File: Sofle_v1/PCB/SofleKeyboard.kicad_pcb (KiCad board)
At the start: 2 copper layers, 137.2 x 109.2 mm, 87 parts, among them J1 LED, J2 4PIN, J3 OLED, P1 i2c_pin, P2 i2c_pin, SW1 SW_PUSH, SW10 SW_PUSH, SW11 SW_PUSH, SW12 SW_PUSH, SW13 SW_PUSH, SW14 SW_PUSH, SW15 SW_PUSH, SW16 SW_PUSH, SW17 SW_PUSH, SW18 SW_PUSH, SW19 SW_PUSH, SW2 SW_PUSH, SW20 SW_PUSH, SW21 SW_PUSH, SW22 SW_PUSH, SW23 SW_PUSH, SW24 SW_PUSH, SW25 Rotary_Encoder_Switch, SW26 SW_PUSH, SW27 SW_PUSH, SW28 SW_PUSH, SW29 SW_PUSH, SW3 SW_PUSH, SW30 SW_PUSH, SW4 SW_PUSH, SW5 SW_PUSH, SW6 SW_PUSH, SW7 SW_PUSH, SW8 SW_PUSH, SW9 SW_PUSH, U1 ProMicro

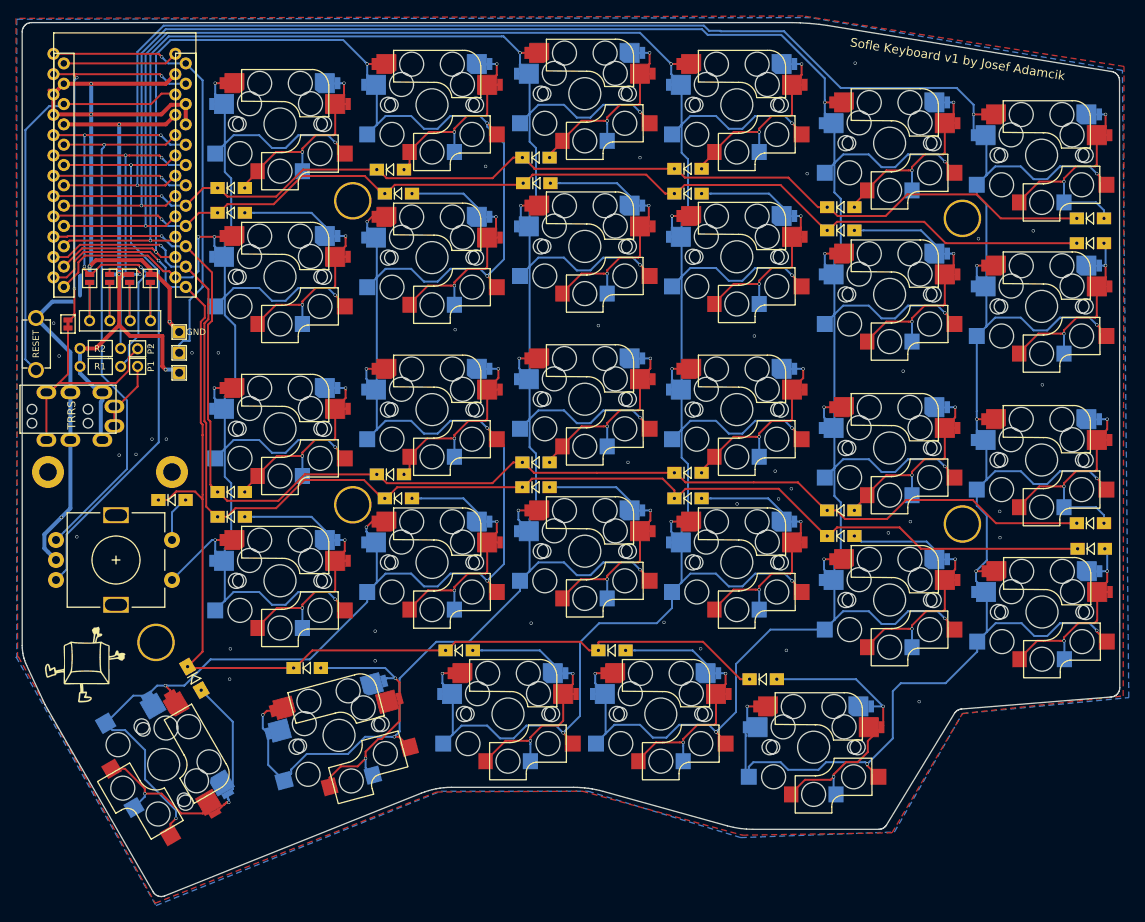
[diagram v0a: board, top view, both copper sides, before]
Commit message: changed footprint to ks 27 reversible
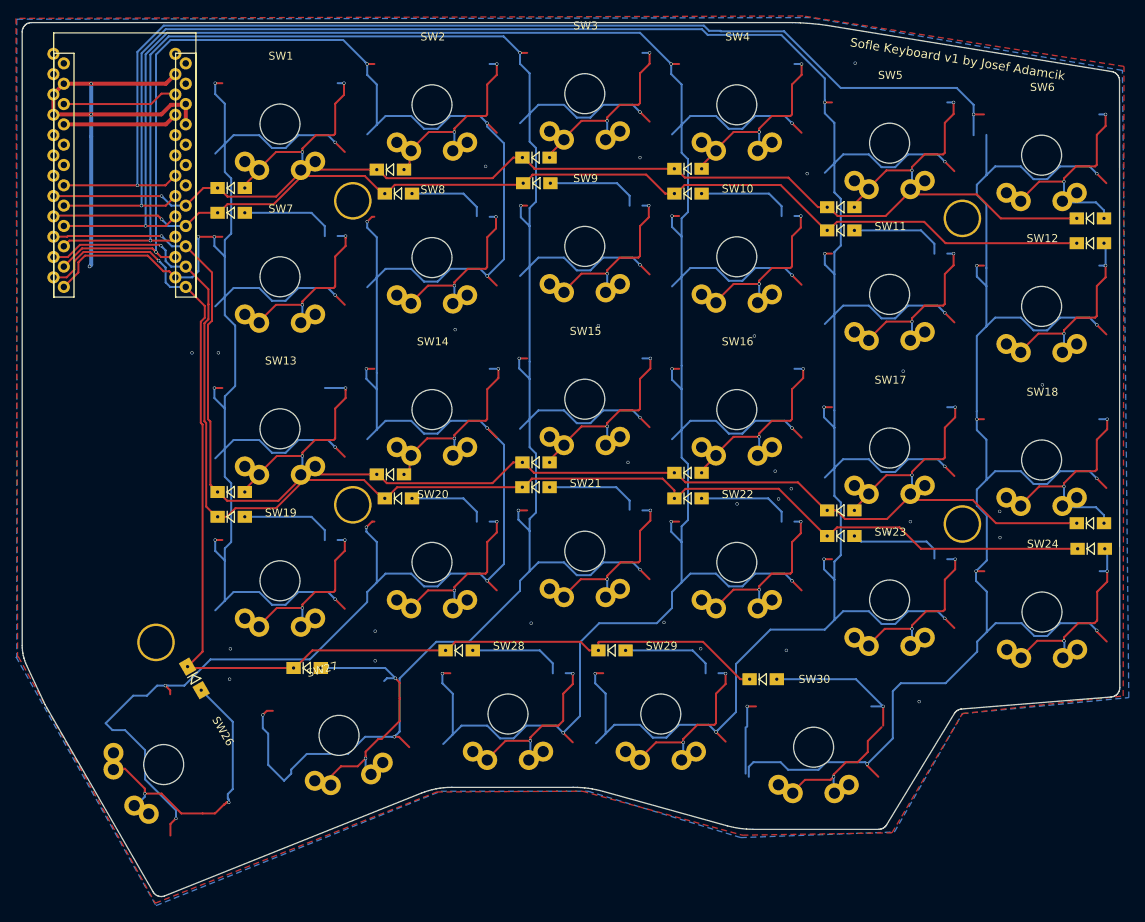
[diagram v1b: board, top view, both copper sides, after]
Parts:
- removed D25: D, SofleKeyboard-footprint:Diode_SOD123
- removed J1: LED, SofleKeyboard-footprint:LED
- removed J2: 4PIN, SofleKeyboard-footprint:MJ-4PP-9
- removed J3: OLED, SofleKeyboard-footprint:OLED_4Pin
- removed JP1, JP2, JP3, JP4, JP5, JP6, JP7, JP8: Jumper_NO_Small, SofleKeyboard-footprint:Jumper
- removed P1, P2: i2c_pin, SofleKeyboard-footprint:1pin_conn
- removed R1, R2: R, SofleKeyboard-footprint:RESISTOR_mini
- removed RSW1: SW_RST, SofleKeyboard-footprint:TACT_SWITCH_TVBP06
- removed Ref** (x2): Val**, SofleKeyboard-footprint:SofleLogoSmall
- removed SW25: Rotary_Encoder_Switch, SofleKeyboard-footprint:RotaryEncoder_Alps_EC11E-Switch_Vertical_H20mm-keebio_modified
- removed TH1, TH2: HOLE, SofleKeyboard-footprint:M2_HOLE_PCB
- removed W1: jumper, SofleKeyboard-footprint:jumper_data
- SW1, SW10, SW11, SW12, SW13, SW14, SW15, SW16, SW17, SW18, SW19, SW2, SW20, SW21, SW22, SW23, SW24, SW27, SW28, SW29, SW3, SW30, SW4, SW5, SW6, SW7, SW8, SW9: footprint SofleKeyboard-footprint:CherryMX_KailhLowProfile_Hotswap -> KS-27 Switch Module:gateron-ks27-reversible
- SW26: footprint SofleKeyboard-footprint:CherryMX_KailhLowProfile_Hotswap_1.5 -> KS-27 Switch Module:gateron-ks27-reversible
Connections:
- SW1 pad 1: SW25A -> col5
- SW13 pad 1: SW25A -> col5
- SW19 pad 1: SW25A -> col5
- SW7 pad 1: SW25A -> col5
- U1 pad 1: LED -> unconnected-(U1-Pad1)
- U1 pad 19: ENCB -> unconnected-(U1-Pad19)
- U1 pad 2: DATA -> unconnected-(U1-Pad2)
- U1 pad 20: ENCA -> unconnected-(U1-Pad20)
- U1 pad 24: Net-(U1-Pad24) -> unconnected-(U1-Pad24)
- U1 pad 5: SDA -> unconnected-(U1-Pad5)
- U1 pad 6: SCL -> unconnected-(U1-Pad6)
- U1 pad 7: Net-(U1-Pad7) -> unconnected-(U1-Pad7)
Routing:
- net row2: track 165.8 -> 384.3 mm, vias 1 -> 6
- net row0: track 138.2 -> 322.3 mm, vias 1 -> 6
- net row3: track 170.1 -> 0.00 mm, vias 1 -> 0
- net row1: track 138.3 -> 0.00 mm, vias 1 -> 0
- net ENCB: track 73.1 -> 0.00 mm, vias 1 -> 0
- net ENCA: track 69.0 -> 0.00 mm, vias 1 -> 0
- net GND: track 124.4 -> 61.2 mm, vias 45 -> 32
- net VCC: track 74.2 -> 14.4 mm, vias 3 -> 0
- net SDA: track 57.0 -> 0.00 mm, vias 4 -> 0
- net LED: track 55.8 -> 0.00 mm, vias 1 -> 0
- net SCL: track 50.1 -> 0.00 mm, vias 3 -> 0
- net DATA: track 48.8 -> 0.00 mm, vias 3 -> 0
- net RESET: track 51.2 -> 14.5 mm
- net /i2c_d: track 29.6 -> 0.00 mm
- net Net-(D13-Pad2): track 28.1 -> 0.00 mm, vias 2 -> 0
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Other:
- net class Default removed
- net class GND removed
- net class VCC removed
